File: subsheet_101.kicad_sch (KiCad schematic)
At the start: 7 parts, among them J03 Jumper wire, J04 Jumper wire

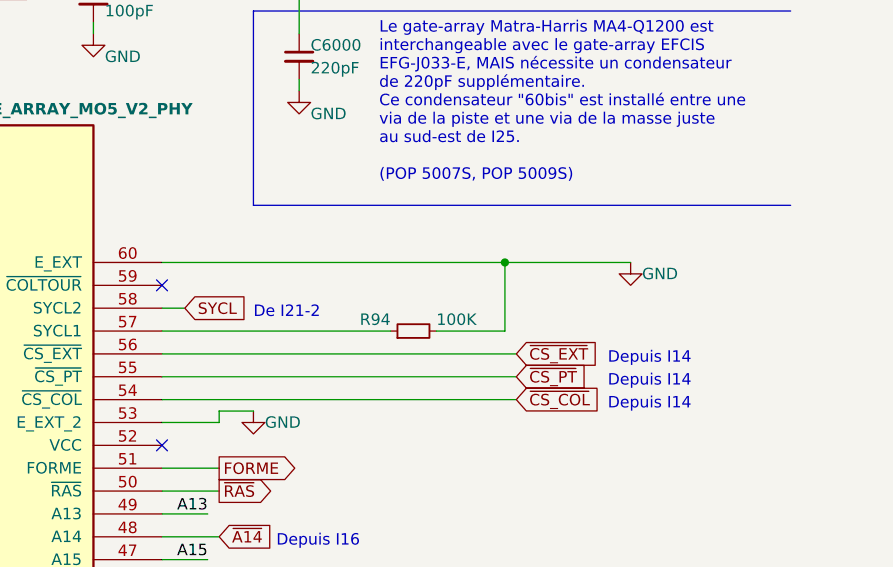
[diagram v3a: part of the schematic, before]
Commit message: Done #20 : missing capacitors C65, C69, C70, C80 (footprints on PCB, not found on schematics)
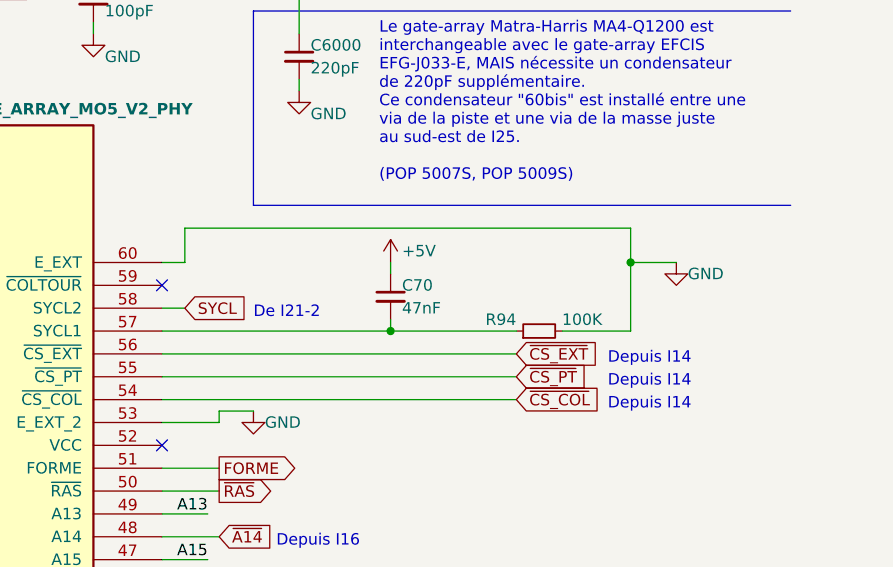
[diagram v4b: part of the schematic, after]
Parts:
- added C70: 47nF, commons-passives_THT:Passive_THT_capacitor_mlcc_W2.54mm_L5.08mm, symbol Device:C_Small
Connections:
- net +5V: now also C70.1
- net at I29.57 (SYCL1), R94.1: now also C70.2
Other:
- moved on the sheet: R94
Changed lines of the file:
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@@
   (junction (at 77.47 177.8) (diameter 0) (color 0 0 0 0)
   )
-  (junction (at 163.83 93.98) (diameter 0) (color 0 0 0 0)
-  )
   (junction (at 82.55 52.07) (diameter 0) (color 0 0 0 0)
   )
@@
   )
   (junction (at 140.97 60.96) (diameter 0) (color 0 0 0 0)
+  )
+  (junction (at 177.8 93.98) (diameter 0) (color 0 0 0 0)
+  )
+  (junction (at 151.13 101.6) (diameter 0) (color 0 0 0 0)
   )
   (junction (at 80.01 68.58) (diameter 0) (color 0 0 0 0)
@@
     (stroke (width 0) (type default))
   )
-  (wire (pts (xy 156.21 101.6) (xy 163.83 101.6))
+  (wire (pts (xy 170.18 101.6) (xy 177.8 101.6))
     (stroke (width 0) (type default))
   )
@@
     (stroke (width 0) (type default))
   )
-  (wire (pts (xy 163.83 101.6) (xy 163.83 93.98))
+  (wire (pts (xy 177.8 101.6) (xy 177.8 93.98))
     (stroke (width 0) (type default))
   )
@@
     (stroke (width 0) (type default))
   )
-  (wire (pts (xy 125.73 93.98) (xy 163.83 93.98))
-    (stroke (width 0) (type default))
-  )
   (wire (pts (xy 95.25 58.42) (xy 95.25 71.12))
     (stroke (width 0) (type default))
@@
     (stroke (width 0) (type default))
   )
-  (wire (pts (xy 163.83 93.98) (xy 177.8 93.98))
+  (wire (pts (xy 177.8 93.98) (xy 182.88 93.98))
     (stroke (width 0) (type default))
   )
@@
     (stroke (width 0) (type default))
   )
+  (wire (pts (xy 128.27 93.98) (xy 125.73 93.98))
+    (stroke (width 0) (type default))
+  )
   (wire (pts (xy 69.85 64.77) (xy 69.85 71.12))
     (stroke (width 0) (type default))
@@
     (stroke (width 0) (type default))
   )
+  (wire (pts (xy 128.27 90.17) (xy 128.27 93.98))
+    (stroke (width 0) (type default))
+  )
   (wire (pts (xy 125.73 127) (xy 130.81 127))
     (stroke (width 0) (type default))
   )
+  (wire (pts (xy 128.27 90.17) (xy 177.8 90.17))
+    (stroke (width 0) (type default))
+  )
   (wire (pts (xy 80.01 157.48) (xy 80.01 163.83))
     (stroke (width 0) (type default))
@@
     (stroke (width 0) (type default))
   )
+  (wire (pts (xy 151.13 93.98) (xy 151.13 95.25))
+    (stroke (width 0) (type default))
+  )
   (wire (pts (xy 95.25 157.48) (xy 95.25 180.34))
     (stroke (width 0) (type default))
@@
     (stroke (width 0) (type default))
   )
+  (wire (pts (xy 177.8 90.17) (xy 177.8 93.98))
+    (stroke (width 0) (type default))
+  )
   (wire (pts (xy 125.73 134.62) (xy 132.08 134.62))
     (stroke (width 0) (type default))
@@
     (stroke (width 0) (type default))
   )
+  (wire (pts (xy 151.13 101.6) (xy 165.1 101.6))
+    (stroke (width 0) (type default))
+  )
   (wire (pts (xy 67.31 54.61) (xy 69.85 54.61))
     (stroke (width 0) (type default))
@@
   )
   (wire (pts (xy 58.42 205.74) (xy 77.47 205.74))
+    (stroke (width 0) (type default))
+  )
+  (wire (pts (xy 151.13 100.33) (xy 151.13 101.6))
     (stroke (width 0) (type default))
   )
@@
     )
   )
+  (symbol (lib_id "power:+5V") (at 151.13 93.98 0) (unit 1)
+    (in_bom yes) (on_board yes) (dnp no)
+    (property "Reference" "#PWR033" (at 151.13 97.79 0)
+      (effects (font (size 1.27 1.27)) hide)
+    )
+    (property "Value" "+5V" (at 152.4 92.71 0)
+      (effects (font (size 1.27 1.27)) (justify left))
+    )
+    (property "Footprint" "" (at 151.13 93.98 0)
+      (effects (font (size 1.27 1.27)) hide)
+    )
+    (property "Datasheet" "" (at 151.13 93.98 0)
+      (effects (font (size 1.27 1.27)) hide)
+    )
+    (pin "1")
+    (instances
+      (project "UC-50-001"
+        (path "/e63e39d7-6ac0-4ffd-8aa3-1841a4541b55/f465a4b1-7c3c-40cc-9e66-ff9f17003d42"
+          (reference "#PWR033") (unit 1)
+        )
+      )
+    )
+  )
   (symbol (lib_id "Device:C_Small") (at 140.97 71.12 0) (unit 1)
     (in_bom yes) (on_board yes) (dnp no)
@@
     )
   )
-  (symbol (lib_id "Device:R_Small") (at 153.67 101.6 90) (unit 1)
-    (in_bom yes) (on_board yes) (dnp no)
-    (property "Reference" "R94" (at 151.13 100.33 90)
-      (effects (font (size 1.27 1.27)) (justify left))
-    )
-    (property "Value" "100K" (at 156.21 100.33 90)
+  (symbol (lib_id "Device:R_Small") (at 167.64 101.6 90) (unit 1)
+    (in_bom yes) (on_board yes) (dnp no)
+    (property "Reference" "R94" (at 165.1 100.33 90)
+      (effects (font (size 1.27 1.27)) (justify left))
+    )
+    (property "Value" "100K" (at 170.18 100.33 90)
       (effects (font (size 1.27 1.27)) (justify right))
     )
-    (property "Footprint" "commons-passives_THT:Passive_THT_resistor_EU_W2.54mm_L12.70mm" (at 153.67 101.6 0)
-      (effects (font (size 1.27 1.27)) hide)
-    )
-    (property "Datasheet" "~" (at 153.67 101.6 0)
+    (property "Footprint" "commons-passives_THT:Passive_THT_resistor_EU_W2.54mm_L12.70mm" (at 167.64 101.6 0)
+      (effects (font (size 1.27 1.27)) hide)
+    )
+    (property "Datasheet" "~" (at 167.64 101.6 0)
       (effects (font (size 1.27 1.27)) hide)
     )
@@
     )
   )
-  (symbol (lib_id "power:GND") (at 177.8 93.98 0) (unit 1)
-    (in_bom yes) (on_board yes) (dnp no)
-    (property "Reference" "#PWR05" (at 177.8 100.33 0)
-      (effects (font (size 1.27 1.27)) hide)
-    )
-    (property "Value" "GND" (at 179.07 95.25 0)
-      (effects (font (size 1.27 1.27)) (justify left))
-    )
-    (property "Footprint" "" (at 177.8 93.98 0)
-      (effects (font (size 1.27 1.27)) hide)
-    )
-    (property "Datasheet" "" (at 177.8 93.98 0)
+  (symbol (lib_id "power:GND") (at 182.88 93.98 0) (unit 1)
+    (in_bom yes) (on_board yes) (dnp no)
+    (property "Reference" "#PWR05" (at 182.88 100.33 0)
+      (effects (font (size 1.27 1.27)) hide)
+    )
+    (property "Value" "GND" (at 184.15 95.25 0)
+      (effects (font (size 1.27 1.27)) (justify left))
+    )
+    (property "Footprint" "" (at 182.88 93.98 0)
+      (effects (font (size 1.27 1.27)) hide)
+    )
+    (property "Datasheet" "" (at 182.88 93.98 0)
       (effects (font (size 1.27 1.27)) hide)
     )
@@
         )
       )
+    )
+  )
+  (symbol (lib_id "Device:C_Small") (at 151.13 97.79 0) (unit 1)
+    (in_bom yes) (on_board yes) (dnp no)
+    (property "Reference" "C70" (at 152.4 96.52 0)
+      (effects (font (size 1.27 1.27)) (justify left))
+    )
+    (property "Value" "47nF" (at 152.4 99.06 0)
+      (effects (font (size 1.27 1.27)) (justify left))
+    )
+    (property "Footprint" "commons-passives_THT:Passive_THT_capacitor_mlcc_W2.54mm_L5.08mm" (at 151.13 97.79 0)
+      (effects (font (size 1.27 1.27)) hide)
+    )
+    (property "Datasheet" "~" (at 151.13 97.79 0)
+      (effects (font (size 1.27 1.27)) hide)
+    )
+    (pin "1")
+    (pin "2")
+    (instances
+      (project "UC-50-001"
+        (path "/e63e39d7-6ac0-4ffd-8aa3-1841a4541b55/f465a4b1-7c3c-40cc-9e66-ff9f17003d42"
+          (reference "C70") (unit 1)
+        )
+      )

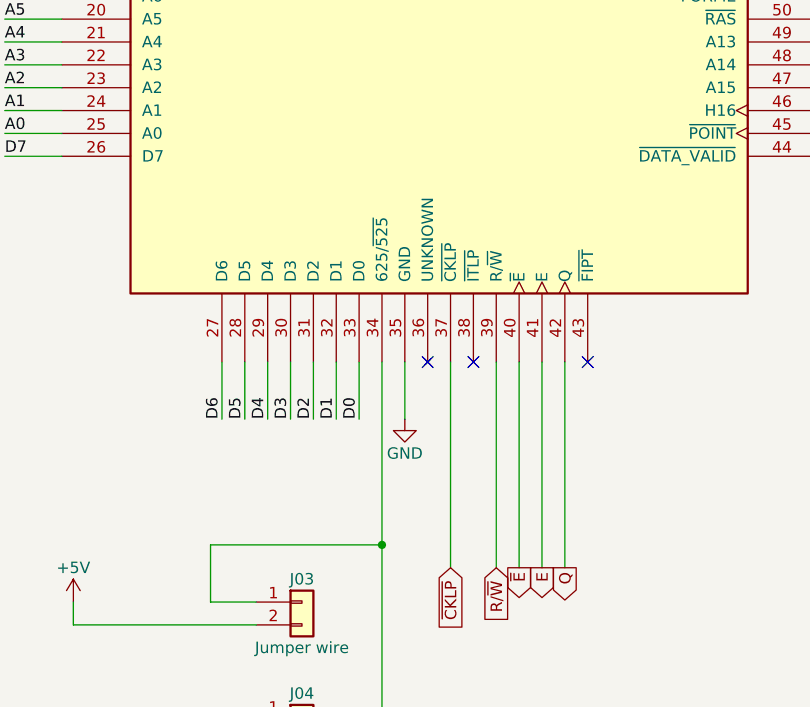
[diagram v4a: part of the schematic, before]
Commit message: Fixed gate array v2 : switched pin 34 and pin 36
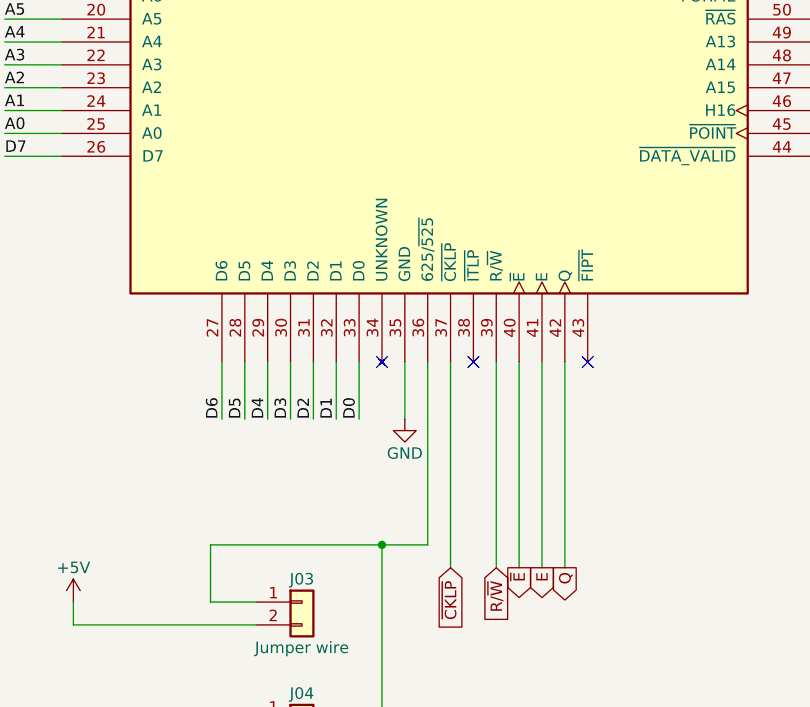
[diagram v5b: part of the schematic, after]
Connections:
- net at J03.1 (Pin_1), J04.2 (Pin_2): now also I29.36 (625/~{525}); no longer I29.34 (625/~{525})
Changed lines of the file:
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@@
   (no_connect (at 125.73 114.3))
   (no_connect (at 100.33 157.48))
+  (no_connect (at 77.47 157.48))
   (no_connect (at 125.73 96.52))
-  (no_connect (at 82.55 157.48))
   (no_connect (at 87.63 157.48))
   (wire (pts (xy 35.56 93.98) (xy 41.91 93.98))
@@
     (stroke (width 0) (type default))
   )
+  (wire (pts (xy 82.55 157.48) (xy 82.55 177.8))
+    (stroke (width 0) (type default))
+  )
   (wire (pts (xy 59.69 64.77) (xy 59.69 71.12))
     (stroke (width 0) (type default))
@@
     (stroke (width 0) (type default))
   )
+  (wire (pts (xy 82.55 177.8) (xy 77.47 177.8))
+    (stroke (width 0) (type default))
+  )
   (wire (pts (xy 125.73 127) (xy 130.81 127))
     (stroke (width 0) (type default))
@@
     (stroke (width 0) (type default))
   )
-  (wire (pts (xy 77.47 157.48) (xy 77.47 177.8))
-    (stroke (width 0) (type default))
-  )

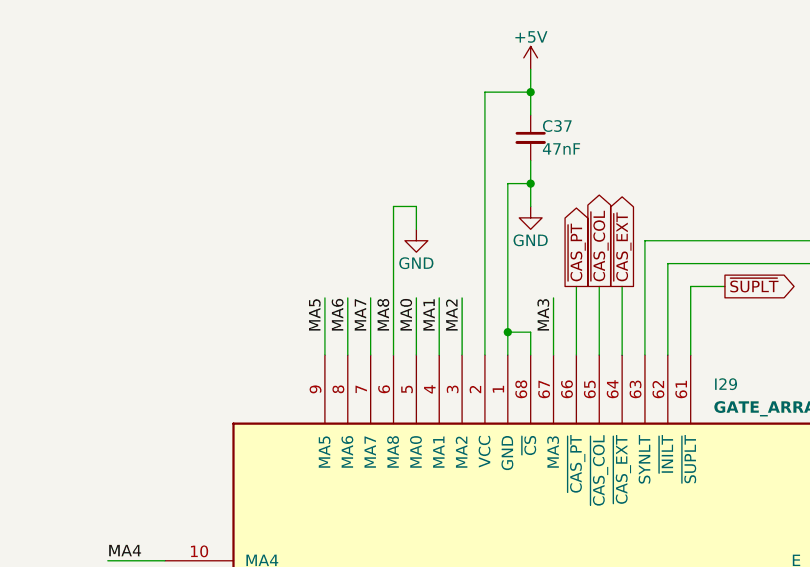
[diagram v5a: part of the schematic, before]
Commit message: Done gate-array, updated some disconnections from pcb into schematic
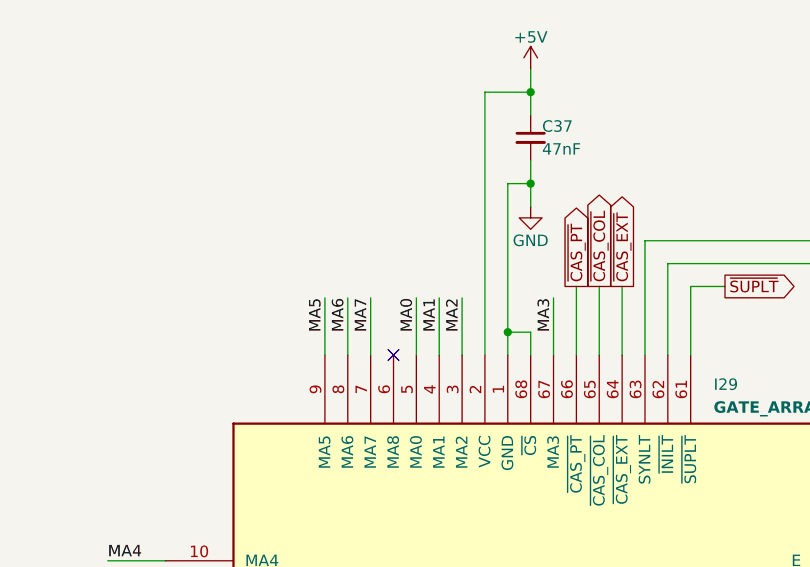
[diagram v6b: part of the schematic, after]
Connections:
- net GND: no longer I29.6 (MA8)
- no-connect marks 5 -> 6
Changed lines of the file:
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@@
   (no_connect (at 125.73 114.3))
   (no_connect (at 100.33 157.48))
+  (no_connect (at 67.31 71.12))
   (no_connect (at 77.47 157.48))
   (no_connect (at 125.73 96.52))
@@
     (stroke (width 0) (type default))
   )
-  (wire (pts (xy 67.31 54.61) (xy 67.31 71.12))
-    (stroke (width 0) (type default))
-  )
   (wire (pts (xy 140.97 73.66) (xy 140.97 74.93))
     (stroke (width 0) (type default))
@@
     (stroke (width 0) (type default))
   )
-  (wire (pts (xy 69.85 54.61) (xy 69.85 57.15))
-    (stroke (width 0) (type default))
-  )
   (wire (pts (xy 151.13 93.98) (xy 151.13 95.25))
     (stroke (width 0) (type default))
@@
   )
   (wire (pts (xy 151.13 101.6) (xy 165.1 101.6))
-    (stroke (width 0) (type default))
-  )
-  (wire (pts (xy 67.31 54.61) (xy 69.85 54.61))
     (stroke (width 0) (type default))
   )
@@
   (label "MA4" (at 35.56 93.98 0) (fields_autoplaced)
     (effects (font (size 1.27 1.27)) (justify left bottom))
-  )
-  (label "MA8" (at 67.31 64.77 270) (fields_autoplaced)
-    (effects (font (size 1.27 1.27)) (justify right bottom))
   )
   (label "MA7" (at 64.77 64.77 270) (fields_autoplaced)
@@
         )
       )
-    )
-  )
-  (symbol (lib_id "power:GND") (at 69.85 57.15 0) (unit 1)
-    (in_bom yes) (on_board yes) (dnp no)
-    (property "Reference" "#PWR07" (at 69.85 63.5 0)
-      (effects (font (size 1.27 1.27)) hide)
-    )
-    (property "Value" "GND" (at 69.85 60.96 0)
-      (effects (font (size 1.27 1.27)))
-    )
-    (property "Footprint" "" (at 69.85 57.15 0)
-      (effects (font (size 1.27 1.27)) hide)
-    )
-    (property "Datasheet" "" (at 69.85 57.15 0)
-      (effects (font (size 1.27 1.27)) hide)
-    )
-    (pin "1")
-    (instances
-      (project "UC-50-001"
-        (path "/e63e39d7-6ac0-4ffd-8aa3-1841a4541b55/f465a4b1-7c3c-40cc-9e66-ff9f17003d42"
-          (reference "#PWR07") (unit 1)
-        )
-      )
